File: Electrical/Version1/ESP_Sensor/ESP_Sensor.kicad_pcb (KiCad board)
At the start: 2 copper layers, 44 parts, among them J1 Power 5V-24V, J2 Programming serial IO, J3 Conn_01x08_Female, Q1 BC817, Q2 BC817, Q3 BC817, Q4 BC817, SW1 Reset, SW2 Prog, U1 TLP291-4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

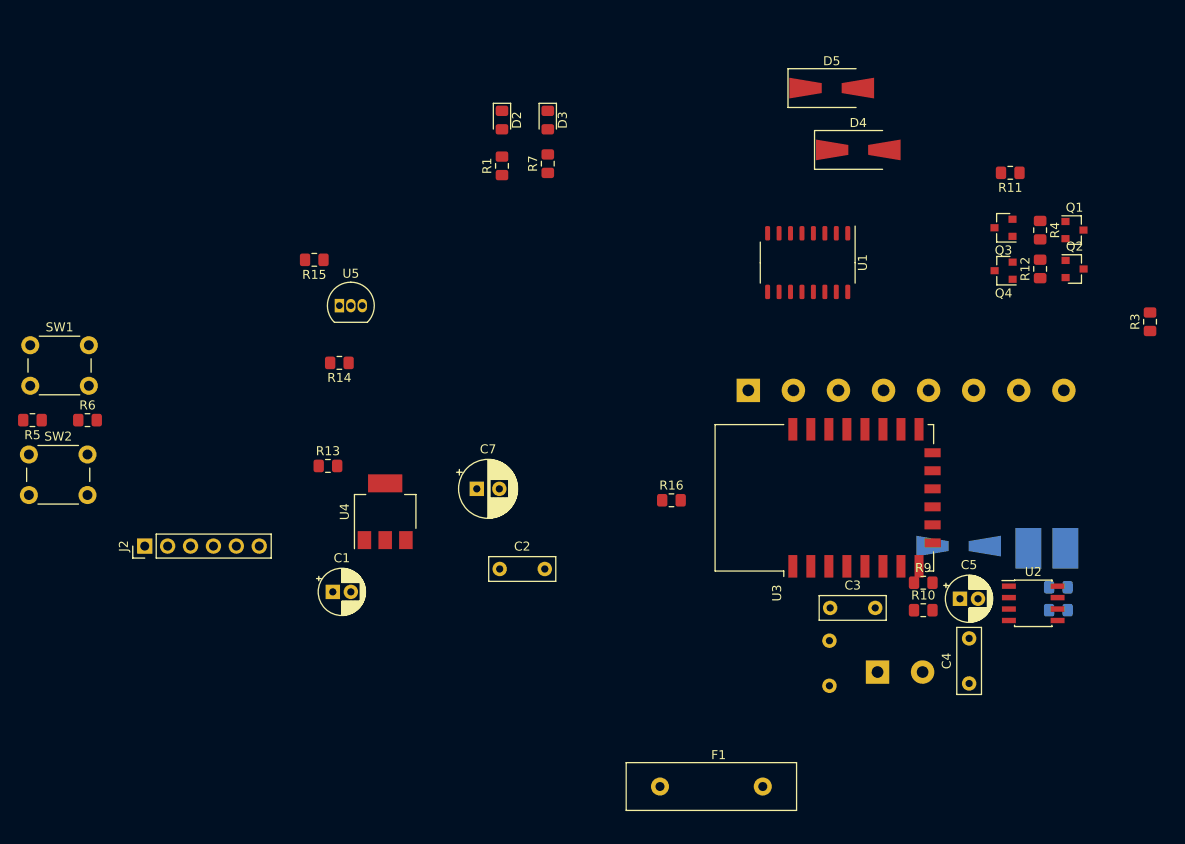
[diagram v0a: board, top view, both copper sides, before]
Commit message: Updated pcb board with smd caps
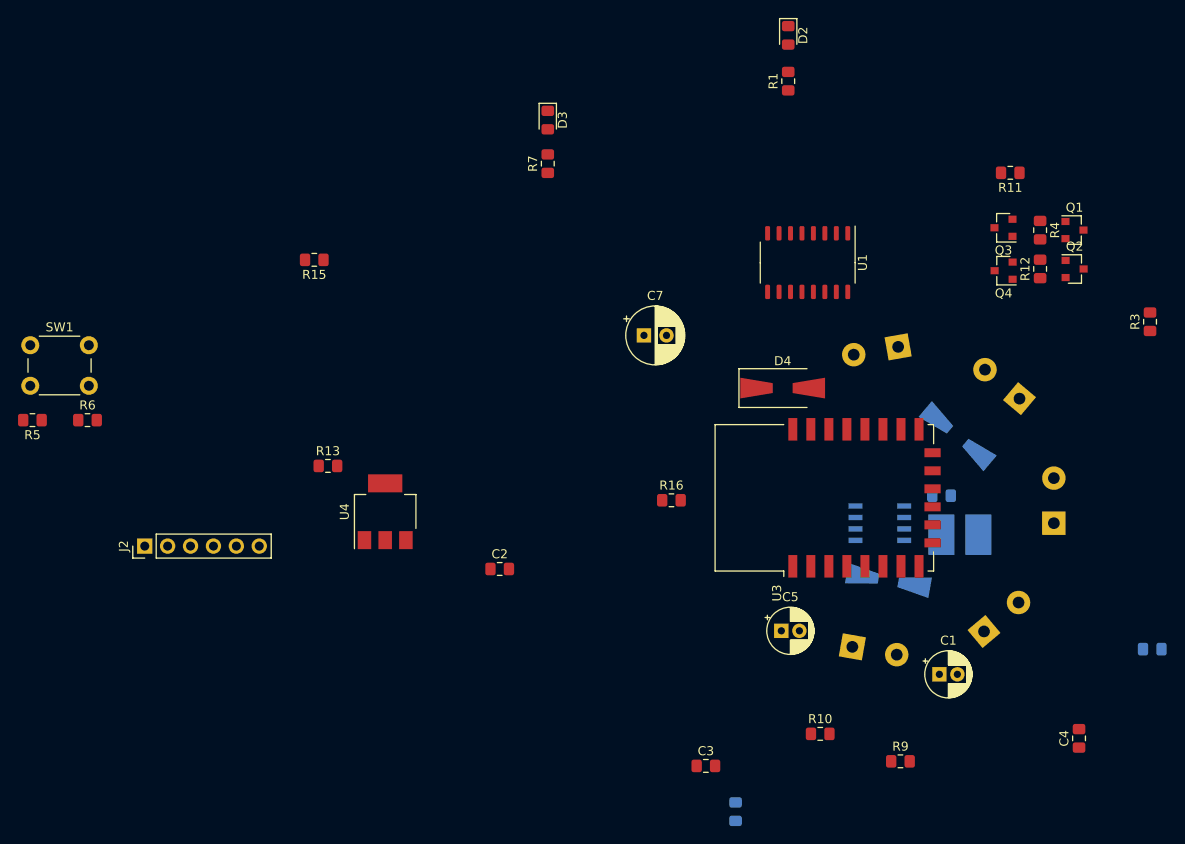
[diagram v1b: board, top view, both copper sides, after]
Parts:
- removed F1: Fuse, Fuse:Fuse_Littelfuse-LVR100
- removed R14: 4k7, Resistor_SMD:R_0805_2012Metric_Pad1.15x1.40mm_HandSolder
- removed SW2: Prog, Button_Switch_THT:SW_PUSH_6mm_H7.3mm
- removed U5: DS18B20, Package_TO_SOT_THT:TO-92_Inline
- added J4: Out 2, TerminalBlock_Phoenix:TerminalBlock_Phoenix_MKDS-1,5-2_1x02_P5.00mm_Horizontal, B.Cu at (177.0, 100.5)
- added J5: In 1, TerminalBlock_Phoenix:TerminalBlock_Phoenix_MKDS-1,5-2_1x02_P5.00mm_Horizontal, B.Cu at (180.8, 114.3)
- added J6: In 2, TerminalBlock_Phoenix:TerminalBlock_Phoenix_MKDS-1,5-2_1x02_P5.00mm_Horizontal, B.Cu at (173.1, 126.3)
- C2, C3, C4, C8: footprint Capacitor_THT:C_Rect_L7.2mm_W2.5mm_P5.00mm_FKS2_FKP2_MKS2_MKP2 -> Capacitor_SMD:C_0805_2012Metric_Pad1.15x1.40mm_HandSolder
- D5, U2: moved to B.Cu
- J2: value Programming serial IO -> Prog IO
- J3: value Conn_01x08_Female -> Out 1; footprint TerminalBlock_Phoenix:TerminalBlock_Phoenix_MKDS-1,5-8_1x08_P5.00mm_Horizontal -> TerminalBlock_Phoenix:TerminalBlock_Phoenix_MKDS-1,5-2_1x02_P5.00mm_Horizontal
- moved C1 67.9 mm to (168.1, 131.1)
- moved D5 41.1 mm to (170.2, 104.6), turned to 140 degrees
- moved D2 33.1 mm to (151.4, 60.2)
- moved R1 33.1 mm to (151.4, 65.3)
- moved D4 27.7 mm to (150.8, 99.3)
- moved C7 25.2 mm to (135.4, 93.5)
- moved C3 22.3 mm to (142.2, 141.2)
- moved C8 21.6 mm to (145.5, 146.3)
- moved C5 20.1 mm to (150.6, 126.2)
- moved R9 20.0 mm to (163.8, 140.7)
- moved U2 19.2 mm to (161.5, 114.3)
- moved R10 17.9 mm to (154.9, 137.7)
- moved J3 17.3 mm to (163.6, 94.7), turned to 190 degrees
- moved R2 16.5 mm to (168.4, 111.3)
- moved C4 13.6 mm to (183.6, 138.2)
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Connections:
- D1 pad 1: Net-(D1-Pad1) -> Net-(C1-Pad1)
- J1 pad 1: Net-(D1-Pad1) -> Net-(C1-Pad1)
- J2 pad 5: Sensor -> ESP_PROG
